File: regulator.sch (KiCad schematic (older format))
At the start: 6 parts, among them U2 LD1117V33

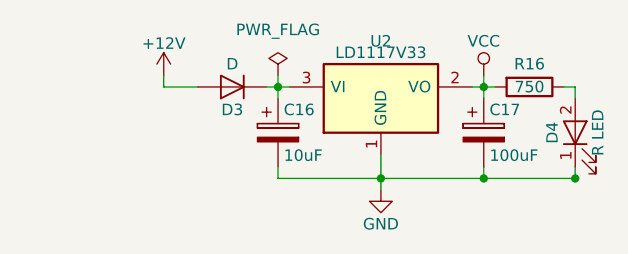
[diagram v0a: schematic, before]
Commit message: Major update to use Atmel ATTINY4313
Replace Pro Micro as microcontroller. Mostly contianed within the
control sheet.
Moved LEDs all onto control sheet.
Updated a few capacitors.
Added a reset switch. Still need to decide part.
Updated a few capacitor models for 4.0.7
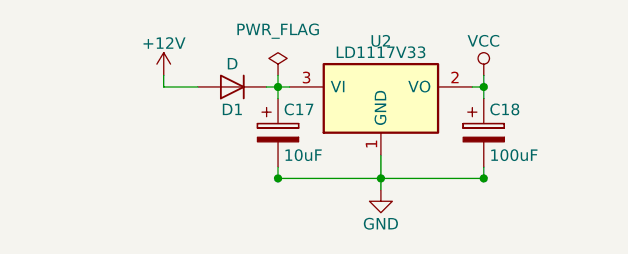
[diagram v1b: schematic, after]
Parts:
- removed D4: R LED, LEDs:LED_D3.0mm_Horizontal_O1.27mm_Z2.0mm, symbol LED
- removed R16: 750, Resistors_THT:R_Axial_DIN0204_L3.6mm_D1.6mm_P5.08mm_Horizontal, symbol R
- U2: footprint TO_SOT_Packages_THT:TO-220_Vertical -> TO_SOT_Packages_THT:TO-220_Horizontal
- renumbered C16 to C17, C17 to C18, D3 to D1
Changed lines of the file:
@@
 $Descr USLetter 11000 8500
 encoding utf-8
-Sheet 10 10
+Sheet 9 10
 Title "Blubaru"
 Date "2017-02-28"
@@
 $EndDescr
 $Comp
-L GND #PWR039
+L GND #PWR034
 U 1 1 59484363
 P 5500 4500
-F 0 "#PWR039" H 5500 4250 50  0001 C CNN
+F 0 "#PWR034" H 5500 4250 50  0001 C CNN
 F 1 "GND" H 5500 4350 50  0000 C CNN
 F 2 "" H 5500 4500 50  0001 C CNN
@@
 	5500 4350 5500 4500
 $Comp
-L +12V #PWR040
+L +12V #PWR035
 U 1 1 59484575
 P 4550 4000
-F 0 "#PWR040" H 4550 3850 50  0001 C CNN
+F 0 "#PWR035" H 4550 3850 50  0001 C CNN
 F 1 "+12V" H 4550 4140 50  0000 C CNN
 F 2 "" H 4550 4000 50  0001 C CNN
@@
 	5950 4000 5950 4100
 $Comp
-L CP C16
+L CP C17
 U 1 1 59484D99
 P 5050 4250
-F 0 "C16" H 5075 4350 50  0000 L CNN
+F 0 "C17" H 5075 4350 50  0000 L CNN
 F 1 "10uF" H 5075 4150 50  0000 L CNN
 F 2 "blubaru:CP_Radial_D4.0mm_P1.50mm" H 5088 4100 50  0001 C CNN
@@
 $EndComp
 $Comp
-L CP C17
+L CP C18
 U 1 1 59484E96
 P 5950 4250
-F 0 "C17" H 5975 4350 50  0000 L CNN
+F 0 "C18" H 5975 4350 50  0000 L CNN
 F 1 "100uF" H 5975 4150 50  0000 L CNN
 F 2 "blubaru:CP_Radial_D6.3mm_P2.50mm" H 5988 4100 50  0001 C CNN
@@
 Connection ~ 5950 4050
 $Comp
-L VCC #PWR041
+L VCC #PWR036
 U 1 1 59486886
 P 5950 4000
-F 0 "#PWR041" H 5950 3850 50  0001 C CNN
+F 0 "#PWR036" H 5950 3850 50  0001 C CNN
 F 1 "VCC" H 5950 4150 50  0000 C CNN
 F 2 "" H 5950 4000 50  0001 C CNN
@@
 F 0 "U2" H 5500 4350 50  0000 C CNN
 F 1 "LD1117V33" H 5500 4300 50  0000 C CNN
-F 2 "TO_SOT_Packages_THT:TO-220_Vertical" H 5500 4200 50  0001 C CNN
+F 2 "TO_SOT_Packages_THT:TO-220_Horizontal" H 5500 4200 50  0001 C CNN
 F 3 "http://www.st.com/content/ccc/resource/technical/document/datasheet/99/3b/7d/91/91/51/4b/be/CD00000544.pdf/files/CD00000544.pdf/jcr:content/translations/en.CD00000544.pdf" H 5500 4100 50  0001 C CNN
 	1    5500 4100
 	1    0    0    -1
 $EndComp
-Wire Wire Line
-	5900 4050 6000 4050
-$Comp
-L R R16
-U 1 1 594DE951
-P 6150 4050
-F 0 "R16" V 6050 4050 50  0000 C CNN
-F 1 "750" V 6150 4050 50  0000 C CNN
-F 2 "Resistors_THT:R_Axial_DIN0204_L3.6mm_D1.6mm_P5.08mm_Horizontal" V 6080 4050 50  0001 C CNN
-F 3 "https://www.seielect.com/Catalog/SEI-CF_CFM.pdf" H 6150 4050 50  0001 C CNN
-	1    6150 4050
-	0    1    1    0
-$EndComp
-$Comp
-L LED D4
-U 1 1 594DE9F6
-P 6350 4250
-F 0 "D4" H 6350 4350 50  0000 C CNN
-F 1 "R LED" H 6350 4150 50  0000 C CNN
-F 2 "LEDs:LED_D3.0mm_Horizontal_O1.27mm_Z2.0mm" H 6350 4250 50  0001 C CNN
-F 3 "http://www.kingbrightusa.com/images/catalog/SPEC/WP710A10LSECK-J3.pdf" H 6350 4250 50  0001 C CNN
-	1    6350 4250
-	0    -1   -1   0
-$EndComp
-Wire Wire Line
-	6300 4050 6350 4050
-Wire Wire Line
-	6350 4050 6350 4100
-Wire Wire Line
-	6350 4450 6350 4400
 Connection ~ 5950 4450
-Connection ~ 6350 4450
-Wire Wire Line
-	5050 4450 6350 4450
 Wire Wire Line
 	4550 4000 4550 4050
@@
 Connection ~ 5050 4050
 $Comp
-L D D3
+L D D1
 U 1 1 5975834F
 P 4850 4050
-F 0 "D3" H 4850 4150 50  0000 C CNN
+F 0 "D1" H 4850 4150 50  0000 C CNN
 F 1 "D" H 4850 3950 50  0000 C CNN
 F 2 "Diodes_THT:D_DO-41_SOD81_P7.62mm_Horizontal" H 4850 4050 50  0001 C CNN
-F 3 "" H 4850 4050 50  0001 C CNN
+F 3 "http://www.onsemi.com/pub/Collateral/1N4001-D.PDF" H 4850 4050 50  0001 C CNN
 	1    4850 4050
 	-1   0    0    1
@@
 	5000 4050 5100 4050
 $Comp
-L PWR_FLAG #FLG042
+L PWR_FLAG #FLG037
 U 1 1 597583E7
 P 5050 4000
-F 0 "#FLG042" H 5050 4075 50  0001 C CNN
+F 0 "#FLG037" H 5050 4075 50  0001 C CNN
 F 1 "PWR_FLAG" H 5050 4200 50  0000 C CNN
 F 2 "" H 5050 4000 50  0001 C CNN
@@
 	1    0    0    -1
 $EndComp
+Wire Wire Line
+	5900 4050 5950 4050
+Connection ~ 5050 4450
+Wire Wire Line
+	5050 4450 5950 4450
 $EndSCHEMATC

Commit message: Add LEDs to BT module
These already exist on the breakout board, but they will be more visible
if I add resistors to the front panel. They can be removed if space is
limited and the case is translucent, but add them for now. In V2, there
won't be a breakout board, so adding them now makes the V1 to V2 fewer
changes.
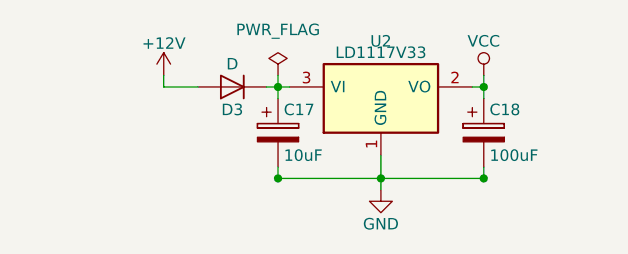
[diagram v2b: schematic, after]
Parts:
- renumbered D1 to D3
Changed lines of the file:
@@
 $EndDescr
 $Comp
-L GND #PWR034
+L GND #PWR035
 U 1 1 59484363
 P 5500 4500
-F 0 "#PWR034" H 5500 4250 50  0001 C CNN
+F 0 "#PWR035" H 5500 4250 50  0001 C CNN
 F 1 "GND" H 5500 4350 50  0000 C CNN
 F 2 "" H 5500 4500 50  0001 C CNN
@@
 	5500 4350 5500 4500
 $Comp
-L +12V #PWR035
+L +12V #PWR036
 U 1 1 59484575
 P 4550 4000
-F 0 "#PWR035" H 4550 3850 50  0001 C CNN
+F 0 "#PWR036" H 4550 3850 50  0001 C CNN
 F 1 "+12V" H 4550 4140 50  0000 C CNN
 F 2 "" H 4550 4000 50  0001 C CNN
@@
 Connection ~ 5950 4050
 $Comp
-L VCC #PWR036
+L VCC #PWR037
 U 1 1 59486886
 P 5950 4000
-F 0 "#PWR036" H 5950 3850 50  0001 C CNN
+F 0 "#PWR037" H 5950 3850 50  0001 C CNN
 F 1 "VCC" H 5950 4150 50  0000 C CNN
 F 2 "" H 5950 4000 50  0001 C CNN
@@
 Connection ~ 5050 4050
 $Comp
-L D D1
+L D D3
 U 1 1 5975834F
 P 4850 4050
-F 0 "D1" H 4850 4150 50  0000 C CNN
+F 0 "D3" H 4850 4150 50  0000 C CNN
 F 1 "D" H 4850 3950 50  0000 C CNN
 F 2 "Diodes_THT:D_DO-41_SOD81_P7.62mm_Horizontal" H 4850 4050 50  0001 C CNN
@@
 	5000 4050 5100 4050
 $Comp
-L PWR_FLAG #FLG037
+L PWR_FLAG #FLG038
 U 1 1 597583E7
 P 5050 4000
-F 0 "#FLG037" H 5050 4075 50  0001 C CNN
+F 0 "#FLG038" H 5050 4075 50  0001 C CNN
 F 1 "PWR_FLAG" H 5050 4200 50  0000 C CNN
 F 2 "" H 5050 4000 50  0001 C CNN

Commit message: Add a better footprint for the regulator
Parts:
- U2: footprint TO_SOT_Packages_THT:TO-220_Horizontal -> blubaru:TO-220_Horizontal
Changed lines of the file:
@@
 F 0 "U2" H 5500 4350 50  0000 C CNN
 F 1 "LD1117V33" H 5500 4300 50  0000 C CNN
-F 2 "TO_SOT_Packages_THT:TO-220_Horizontal" H 5500 4200 50  0001 C CNN
+F 2 "blubaru:TO-220_Horizontal" H 5500 4200 50  0001 C CNN
 F 3 "http://www.st.com/content/ccc/resource/technical/document/datasheet/99/3b/7d/91/91/51/4b/be/CD00000544.pdf/files/CD00000544.pdf/jcr:content/translations/en.CD00000544.pdf" H 5500 4100 50  0001 C CNN
 	1    5500 4100

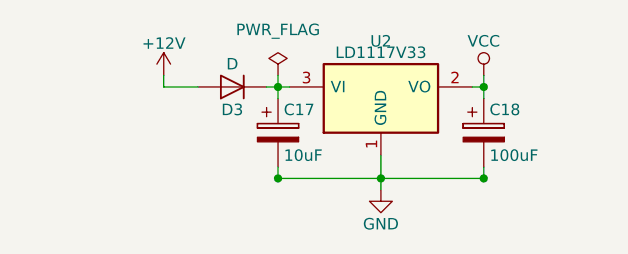
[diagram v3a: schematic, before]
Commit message: Clean up some schematics for readability.
Run 12V from after power protection diode.
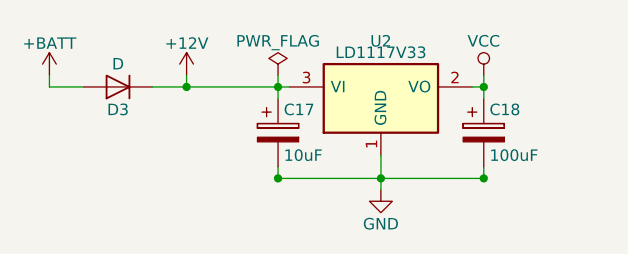
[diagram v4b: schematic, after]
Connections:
- net +12V: now also C17.1, D3.1 (K), U2.3 (VI); no longer D3.2 (A)
- new net +BATT: D3.2 (A)
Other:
- moved on the sheet: D3
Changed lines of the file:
@@
 L +12V #PWR036
 U 1 1 59484575
-P 4550 4000
-F 0 "#PWR036" H 4550 3850 50  0001 C CNN
-F 1 "+12V" H 4550 4140 50  0000 C CNN
-F 2 "" H 4550 4000 50  0001 C CNN
-F 3 "" H 4550 4000 50  0001 C CNN
-	1    4550 4000
+P 4650 4000
+F 0 "#PWR036" H 4650 3850 50  0001 C CNN
+F 1 "+12V" H 4650 4140 50  0000 C CNN
+F 2 "" H 4650 4000 50  0001 C CNN
+F 3 "" H 4650 4000 50  0001 C CNN
+	1    4650 4000
 	1    0    0    -1
 $EndComp
@@
 Connection ~ 5950 4450
 Wire Wire Line
-	4550 4000 4550 4050
+	4050 4000 4050 4050
 Wire Wire Line
-	4550 4050 4700 4050
+	4050 4050 4200 4050
 Wire Wire Line
 	5050 4000 5050 4100
@@
 L D D3
 U 1 1 5975834F
-P 4850 4050
-F 0 "D3" H 4850 4150 50  0000 C CNN
-F 1 "D" H 4850 3950 50  0000 C CNN
-F 2 "Diodes_THT:D_DO-41_SOD81_P7.62mm_Horizontal" H 4850 4050 50  0001 C CNN
-F 3 "http://www.onsemi.com/pub/Collateral/1N4001-D.PDF" H 4850 4050 50  0001 C CNN
-	1    4850 4050
+P 4350 4050
+F 0 "D3" H 4350 4150 50  0000 C CNN
+F 1 "D" H 4350 3950 50  0000 C CNN
+F 2 "Diodes_THT:D_DO-41_SOD81_P7.62mm_Horizontal" H 4350 4050 50  0001 C CNN
+F 3 "http://www.onsemi.com/pub/Collateral/1N4001-D.PDF" H 4350 4050 50  0001 C CNN
+	1    4350 4050
 	-1   0    0    1
 $EndComp
 Wire Wire Line
-	5000 4050 5100 4050
+	4500 4050 5100 4050
+Wire Wire Line
+	5900 4050 5950 4050
+Connection ~ 5050 4450
+Wire Wire Line
+	5050 4450 5950 4450
 $Comp
-L PWR_FLAG #FLG038
-U 1 1 597583E7
+L +BATT #PWR?
+U 1 1 5A376B9B
+P 4050 4000
+F 0 "#PWR?" H 4050 3850 50  0001 C CNN
+F 1 "+BATT" H 4050 4140 50  0000 C CNN
+F 2 "" H 4050 4000 50  0001 C CNN
+F 3 "" H 4050 4000 50  0001 C CNN
+	1    4050 4000
+	1    0    0    -1
+$EndComp
+$Comp
+L PWR_FLAG #FLG?
+U 1 1 5A377031
 P 5050 4000
-F 0 "#FLG038" H 5050 4075 50  0001 C CNN
-F 1 "PWR_FLAG" H 5050 4200 50  0000 C CNN
+F 0 "#FLG?" H 5050 4075 50  0001 C CNN
+F 1 "PWR_FLAG" H 5050 4150 50  0000 C CNN
 F 2 "" H 5050 4000 50  0001 C CNN
 F 3 "" H 5050 4000 50  0001 C CNN
@@
 $EndComp
 Wire Wire Line
-	5900 4050 5950 4050
-Connection ~ 5050 4450
-Wire Wire Line
-	5050 4450 5950 4450
+	4650 4000 4650 4050
+Connection ~ 4650 4050
 $EndSCHEMATC

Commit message: Re-add MCU footprint and use vertical regul.
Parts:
- U2: footprint blubaru:TO-220_Horizontal -> TO_SOT_Packages_THT:TO-220_Vertical
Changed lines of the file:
@@
 F 0 "U2" H 5500 4350 50  0000 C CNN
 F 1 "LD1117V33" H 5500 4300 50  0000 C CNN
-F 2 "blubaru:TO-220_Horizontal" H 5500 4200 50  0001 C CNN
+F 2 "TO_SOT_Packages_THT:TO-220_Vertical" H 5500 4200 50  0001 C CNN
 F 3 "http://www.st.com/content/ccc/resource/technical/document/datasheet/99/3b/7d/91/91/51/4b/be/CD00000544.pdf/files/CD00000544.pdf/jcr:content/translations/en.CD00000544.pdf" H 5500 4100 50  0001 C CNN
 	1    5500 4100

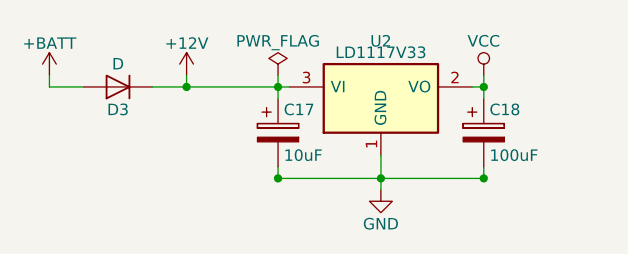
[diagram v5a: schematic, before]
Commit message: Rename the bluetooth reset line
This is needed so it doesn't conflict with the MCU reset line of the
same name. Apparently that puts them on the same net.

Also, reorder the LEDs so they have nicer numbers on the board.
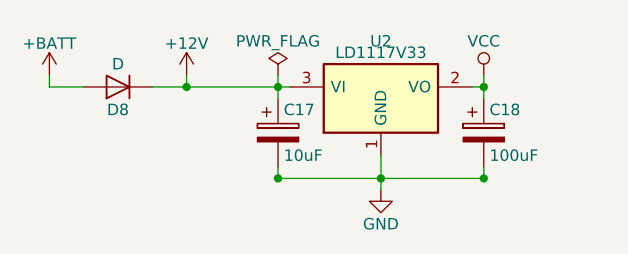
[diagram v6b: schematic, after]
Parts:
- renumbered D3 to D8
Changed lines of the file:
@@
 Connection ~ 5050 4050
 $Comp
-L D D3
+L D D8
 U 1 1 5975834F
 P 4350 4050
-F 0 "D3" H 4350 4150 50  0000 C CNN
+F 0 "D8" H 4350 4150 50  0000 C CNN
 F 1 "D" H 4350 3950 50  0000 C CNN
 F 2 "Diodes_THT:D_DO-41_SOD81_P7.62mm_Horizontal" H 4350 4050 50  0001 C CNN
@@
 	5050 4450 5950 4450
 $Comp
-L +BATT #PWR?
+L +BATT #PWR038
 U 1 1 5A376B9B
 P 4050 4000
-F 0 "#PWR?" H 4050 3850 50  0001 C CNN
+F 0 "#PWR038" H 4050 3850 50  0001 C CNN
 F 1 "+BATT" H 4050 4140 50  0000 C CNN
 F 2 "" H 4050 4000 50  0001 C CNN
@@
 $EndComp
 $Comp
-L PWR_FLAG #FLG?
+L PWR_FLAG #FLG039
 U 1 1 5A377031
 P 5050 4000
-F 0 "#FLG?" H 5050 4075 50  0001 C CNN
+F 0 "#FLG039" H 5050 4075 50  0001 C CNN
 F 1 "PWR_FLAG" H 5050 4150 50  0000 C CNN
 F 2 "" H 5050 4000 50  0001 C CNN
